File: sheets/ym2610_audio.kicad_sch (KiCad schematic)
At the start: 51 parts, among them J3 SMK S-G8043, U25 NJM2016D, U26 YM3016D, U27 YM2610, U28 RC4558, U29 RC4558, U30 RC4558, U31 RC4558

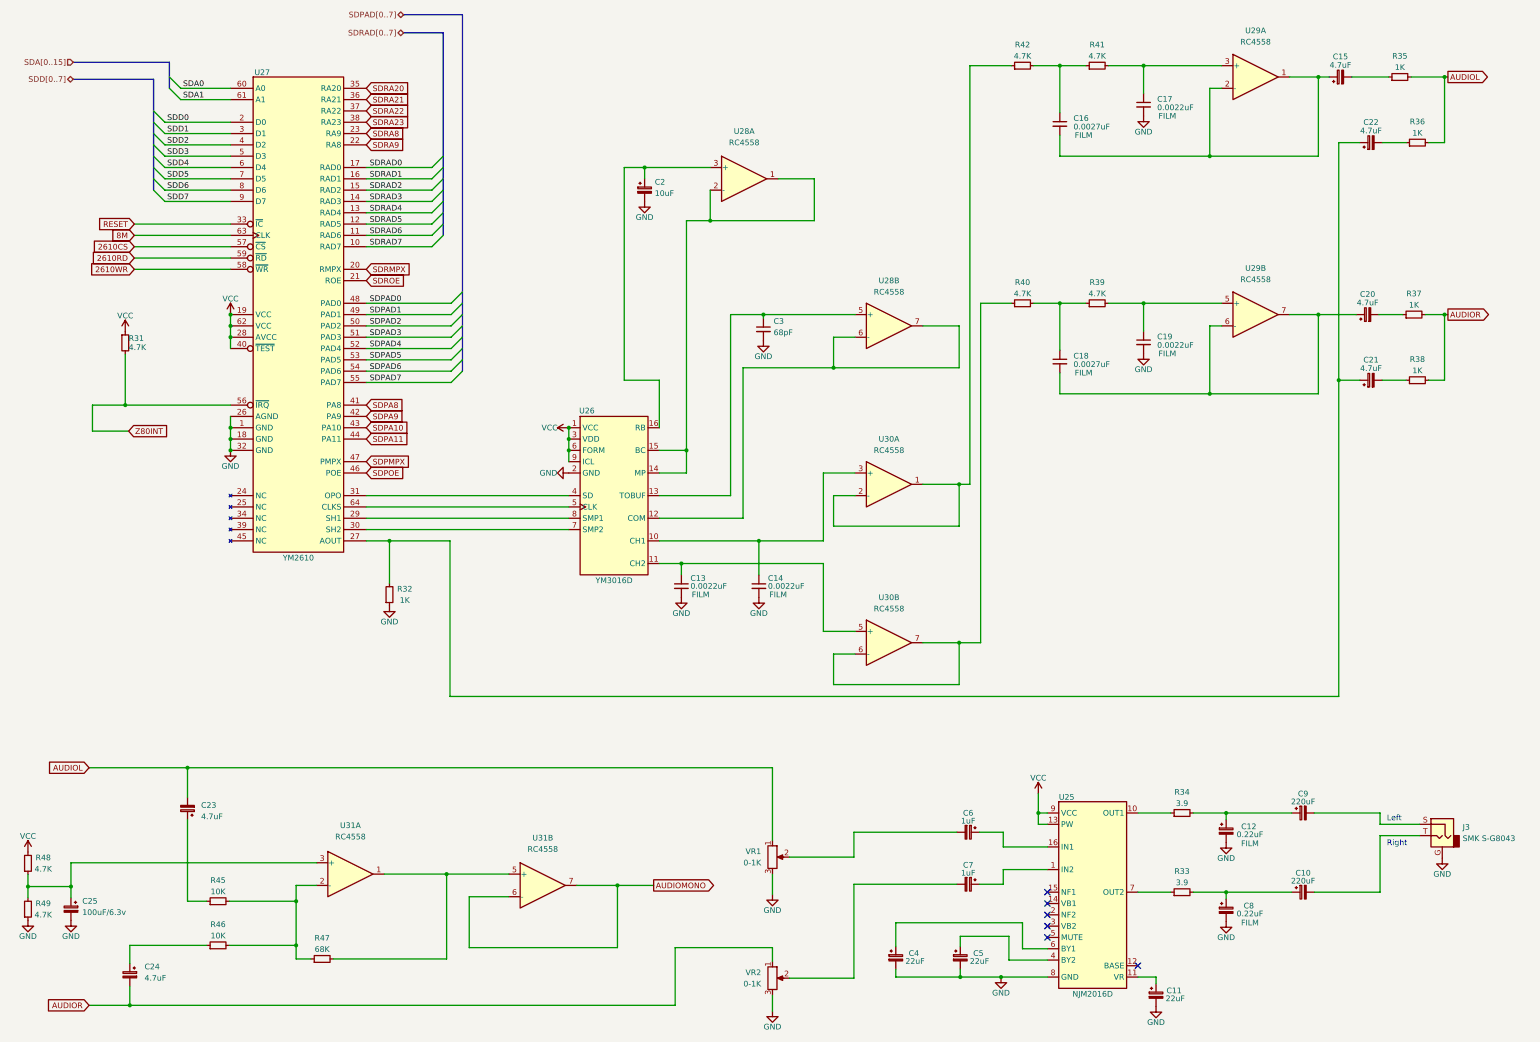
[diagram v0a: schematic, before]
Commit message: Resistor Value Ω added
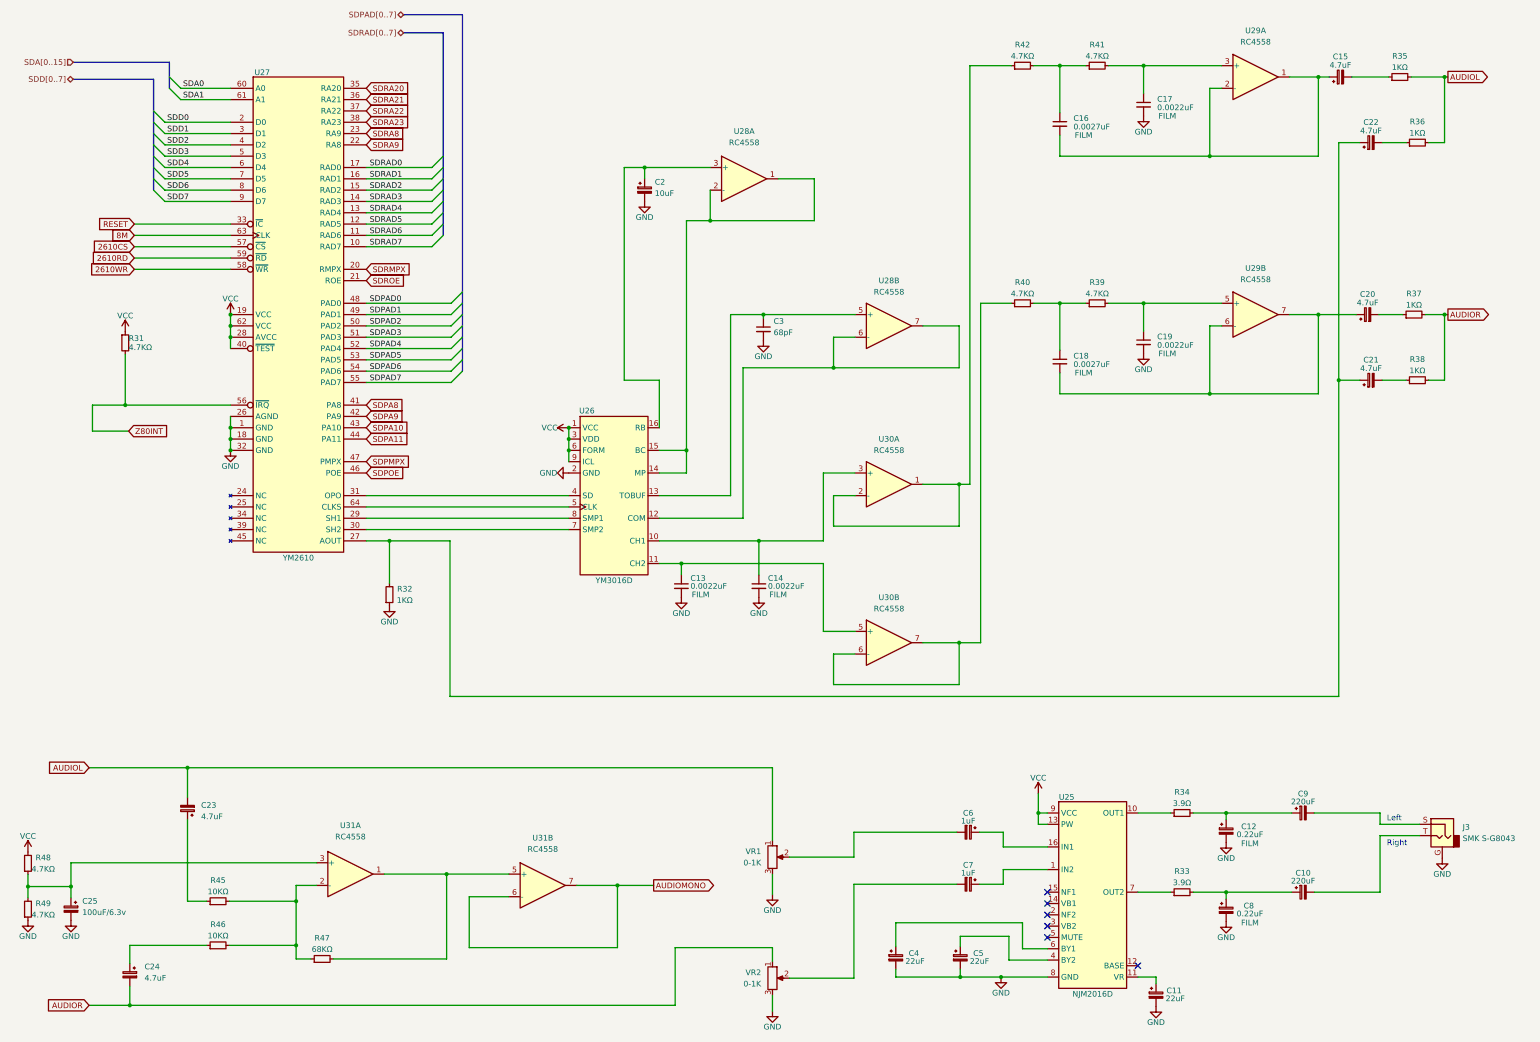
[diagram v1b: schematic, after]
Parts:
- R31, R39, R40, R41, R42, R48, R49: value 4.7K -> 4.7KΩ
- R32, R35, R36, R37, R38: value 1K -> 1KΩ
- R33, R34: value 3.9 -> 3.9Ω
- R45, R46: value 10K -> 10KΩ
- R47: value 68K -> 68KΩ
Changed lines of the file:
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@@
     (in_bom yes) (on_board yes)
     (property "Reference" "R45" (id 0) (at 90.424 211.201 90))
-    (property "Value" "10K" (id 1) (at 90.424 213.741 90))
+    (property "Value" "10KΩ" (id 1) (at 90.424 213.741 90))
     (property "Footprint" "" (id 2) (at 90.424 215.9 0)
       (effects (font (size 1.27 1.27)) hide)
@@
     (in_bom yes) (on_board yes)
     (property "Reference" "R36" (id 0) (at 359.664 40.894 90))
-    (property "Value" "1K" (id 1) (at 359.664 43.434 90))
+    (property "Value" "1KΩ" (id 1) (at 359.664 43.434 90))
     (property "Footprint" "" (id 2) (at 359.664 45.593 0)
       (effects (font (size 1.27 1.27)) hide)
@@
     (in_bom yes) (on_board yes)
     (property "Reference" "R37" (id 0) (at 358.902 79.502 90))
-    (property "Value" "1K" (id 1) (at 358.902 82.042 90))
+    (property "Value" "1KΩ" (id 1) (at 358.902 82.042 90))
     (property "Footprint" "" (id 2) (at 358.902 84.201 0)
       (effects (font (size 1.27 1.27)) hide)
@@
     (in_bom yes) (on_board yes)
     (property "Reference" "R38" (id 0) (at 359.664 94.234 90))
-    (property "Value" "1K" (id 1) (at 359.664 96.774 90))
+    (property "Value" "1KΩ" (id 1) (at 359.664 96.774 90))
     (property "Footprint" "" (id 2) (at 359.664 98.933 0)
       (effects (font (size 1.27 1.27)) hide)
@@
     (in_bom yes) (on_board yes)
     (property "Reference" "R47" (id 0) (at 113.792 224.155 90))
-    (property "Value" "68K" (id 1) (at 113.792 226.695 90))
+    (property "Value" "68KΩ" (id 1) (at 113.792 226.695 90))
     (property "Footprint" "" (id 2) (at 113.792 228.854 0)
       (effects (font (size 1.27 1.27)) hide)
@@
     (in_bom yes) (on_board yes)
     (property "Reference" "R42" (id 0) (at 271.018 23.622 90))
-    (property "Value" "4.7K" (id 1) (at 271.018 26.162 90))
+    (property "Value" "4.7KΩ" (id 1) (at 271.018 26.162 90))
     (property "Footprint" "" (id 2) (at 271.018 28.321 0)
       (effects (font (size 1.27 1.27)) hide)
@@
     (in_bom yes) (on_board yes)
     (property "Reference" "R46" (id 0) (at 90.424 221.107 90))
-    (property "Value" "10K" (id 1) (at 90.424 223.647 90))
+    (property "Value" "10KΩ" (id 1) (at 90.424 223.647 90))
     (property "Footprint" "" (id 2) (at 90.424 225.806 0)
       (effects (font (size 1.27 1.27)) hide)
@@
     (in_bom yes) (on_board yes)
     (property "Reference" "R33" (id 0) (at 306.832 209.169 90))
-    (property "Value" "3.9" (id 1) (at 306.832 211.709 90))
+    (property "Value" "3.9Ω" (id 1) (at 306.832 211.709 90))
     (property "Footprint" "" (id 2) (at 306.832 213.868 0)
       (effects (font (size 1.27 1.27)) hide)
@@
     (in_bom yes) (on_board yes)
     (property "Reference" "R34" (id 0) (at 306.832 191.389 90))
-    (property "Value" "3.9" (id 1) (at 306.832 193.929 90))
+    (property "Value" "3.9Ω" (id 1) (at 306.832 193.929 90))
     (property "Footprint" "" (id 2) (at 306.832 196.088 0)
       (effects (font (size 1.27 1.27)) hide)
@@
     (in_bom yes) (on_board yes)
     (property "Reference" "R40" (id 0) (at 271.018 76.962 90))
-    (property "Value" "4.7K" (id 1) (at 271.018 79.502 90))
+    (property "Value" "4.7KΩ" (id 1) (at 271.018 79.502 90))
     (property "Footprint" "" (id 2) (at 271.018 81.661 0)
       (effects (font (size 1.27 1.27)) hide)
@@
       (effects (font (size 1.27 1.27)) (justify left))
     )
-    (property "Value" "4.7K" (id 1) (at 70.358 91.567 0)
+    (property "Value" "4.7KΩ" (id 1) (at 70.358 91.567 0)
       (effects (font (size 1.27 1.27)) (justify left))
     )
@@
     (in_bom yes) (on_board yes)
     (property "Reference" "R39" (id 0) (at 287.782 76.962 90))
-    (property "Value" "4.7K" (id 1) (at 287.782 79.502 90))
+    (property "Value" "4.7KΩ" (id 1) (at 287.782 79.502 90))
     (property "Footprint" "" (id 2) (at 287.782 81.661 0)
       (effects (font (size 1.27 1.27)) hide)
@@
     (in_bom yes) (on_board yes)
     (property "Reference" "R41" (id 0) (at 287.782 23.622 90))
-    (property "Value" "4.7K" (id 1) (at 287.782 26.162 90))
+    (property "Value" "4.7KΩ" (id 1) (at 287.782 26.162 90))
     (property "Footprint" "" (id 2) (at 287.782 28.321 0)
       (effects (font (size 1.27 1.27)) hide)
@@
     (in_bom yes) (on_board yes)
     (property "Reference" "R48" (id 0) (at 51.181 206.121 0))
-    (property "Value" "4.7K" (id 1) (at 51.181 208.661 0))
+    (property "Value" "4.7KΩ" (id 1) (at 51.181 208.661 0))
     (property "Footprint" "" (id 2) (at 47.752 207.391 0)
       (effects (font (size 1.27 1.27)) hide)
@@
     (in_bom yes) (on_board yes)
     (property "Reference" "R32" (id 0) (at 132.334 145.796 0))
-    (property "Value" "1K" (id 1) (at 132.334 148.336 0))
+    (property "Value" "1KΩ" (id 1) (at 132.334 148.336 0))
     (property "Footprint" "" (id 2) (at 128.905 147.066 0)
       (effects (font (size 1.27 1.27)) hide)
@@
     (in_bom yes) (on_board yes)
     (property "Reference" "R35" (id 0) (at 355.727 26.162 90))
-    (property "Value" "1K" (id 1) (at 355.727 28.702 90))
+    (property "Value" "1KΩ" (id 1) (at 355.727 28.702 90))
     (property "Footprint" "" (id 2) (at 355.727 30.861 0)
       (effects (font (size 1.27 1.27)) hide)
@@
     (in_bom yes) (on_board yes)
     (property "Reference" "R49" (id 0) (at 51.181 216.408 0))
-    (property "Value" "4.7K" (id 1) (at 51.181 218.948 0))
+    (property "Value" "4.7KΩ" (id 1) (at 51.181 218.948 0))
     (property "Footprint" "" (id 2) (at 47.752 217.678 0)
       (effects (font (size 1.27 1.27)) hide)

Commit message: Assigning Footprints
Assigned some footprints to some components. Can still be wrong size on caps
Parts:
- C10, C11, C12, C2, C4, C5, C6, C7, C8, C9: footprint (none) -> 1_NeoGeoLibrary:CAP1-5mm
- C13, C14, C15, C16, C17, C18, C19, C20, C21, C22, C23, C24, C25, C3: footprint (none) -> 1_NeoGeoLibrary:CAP3-5mm
- R31, R32, R33, R34, R35, R36, R37, R38, R39, R40, R41, R42, R45, R46, R47, R48, R49: footprint (none) -> 1_NeoGeoLibrary:Resistor1-5mm

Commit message: Updated Footprints
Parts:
- J3: footprint (none) -> Jumper:SolderJumper-2_P1.3mm_Open_Pad1.0x1.5mm
- U25, U26: footprint (none) -> Package_DIP:DIP-16_W7.62mm
- U27: footprint (none) -> Package_DIP:DIP-64_W25.4mm
- U28, U29, U30, U31: footprint (none) -> Package_DIP:DIP-8_W7.62mm
- VR1, VR2: footprint (none) -> Connector_PinSocket_2.54mm:PinSocket_1x03_P2.54mm_Vertical
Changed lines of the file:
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@@
     (property "Reference" "U25" (id 0) (at 280.924 192.532 0))
     (property "Value" "NJM2016D" (id 1) (at 286.766 236.728 0))
-    (property "Footprint" "" (id 2) (at 286.766 218.948 0)
+    (property "Footprint" "Package_DIP:DIP-16_W7.62mm" (id 2) (at 286.766 218.948 0)
       (effects (font (size 1.27 1.27)) hide)
     )
@@
     (property "Reference" "U28" (id 0) (at 241.046 76.581 0))
     (property "Value" "RC4558" (id 1) (at 241.046 79.121 0))
-    (property "Footprint" "" (id 2) (at 241.046 86.741 0)
+    (property "Footprint" "Package_DIP:DIP-8_W7.62mm" (id 2) (at 241.046 86.741 0)
       (effects (font (size 1.27 1.27)) hide)
     )
@@
     (property "Reference" "U30" (id 0) (at 241.046 112.141 0))
     (property "Value" "RC4558" (id 1) (at 241.046 114.681 0))
-    (property "Footprint" "" (id 2) (at 241.046 122.301 0)
+    (property "Footprint" "Package_DIP:DIP-8_W7.62mm" (id 2) (at 241.046 122.301 0)
       (effects (font (size 1.27 1.27)) hide)
     )
@@
     (property "Reference" "U29" (id 0) (at 323.342 20.447 0))
     (property "Value" "RC4558" (id 1) (at 323.342 22.987 0))
-    (property "Footprint" "" (id 2) (at 323.342 30.861 0)
+    (property "Footprint" "Package_DIP:DIP-8_W7.62mm" (id 2) (at 323.342 30.861 0)
       (effects (font (size 1.27 1.27)) hide)
     )
@@
     (property "Reference" "U30" (id 0) (at 241.046 147.701 0))
     (property "Value" "RC4558" (id 1) (at 241.046 150.241 0))
-    (property "Footprint" "" (id 2) (at 241.046 157.861 0)
+    (property "Footprint" "Package_DIP:DIP-8_W7.62mm" (id 2) (at 241.046 157.861 0)
       (effects (font (size 1.27 1.27)) hide)
     )
@@
       (effects (font (size 1.27 1.27)) (justify right))
     )
-    (property "Footprint" "" (id 2) (at 214.884 205.994 0)
+    (property "Footprint" "Connector_PinSocket_2.54mm:PinSocket_1x03_P2.54mm_Vertical" (id 2) (at 214.884 205.994 0)
       (effects (font (size 1.27 1.27)) hide)
     )
@@
     (property "Reference" "U26" (id 0) (at 173.228 105.791 0))
     (property "Value" "YM3016D" (id 1) (at 179.324 143.891 0))
-    (property "Footprint" "" (id 2) (at 179.324 132.461 0)
+    (property "Footprint" "Package_DIP:DIP-16_W7.62mm" (id 2) (at 179.324 132.461 0)
       (effects (font (size 1.27 1.27)) hide)
     )
@@
     (property "Reference" "U29" (id 0) (at 323.342 73.787 0))
     (property "Value" "RC4558" (id 1) (at 323.342 76.327 0))
-    (property "Footprint" "" (id 2) (at 323.342 84.201 0)
+    (property "Footprint" "Package_DIP:DIP-8_W7.62mm" (id 2) (at 323.342 84.201 0)
       (effects (font (size 1.27 1.27)) hide)
     )
@@
     (property "Reference" "U31" (id 0) (at 120.142 198.882 0))
     (property "Value" "RC4558" (id 1) (at 120.142 201.422 0))
-    (property "Footprint" "" (id 2) (at 120.142 209.804 0)
+    (property "Footprint" "Package_DIP:DIP-8_W7.62mm" (id 2) (at 120.142 209.804 0)
       (effects (font (size 1.27 1.27)) hide)
     )
@@
     (property "Reference" "U31" (id 0) (at 163.322 201.676 0))
     (property "Value" "RC4558" (id 1) (at 163.322 204.216 0))
-    (property "Footprint" "" (id 2) (at 163.322 212.344 0)
+    (property "Footprint" "Package_DIP:DIP-8_W7.62mm" (id 2) (at 163.322 212.344 0)
       (effects (font (size 1.27 1.27)) hide)
     )
@@
       (effects (font (size 1.27 1.27)) (justify right))
     )
-    (property "Footprint" "" (id 2) (at 365.252 201.168 0)
+    (property "Footprint" "Jumper:SolderJumper-2_P1.3mm_Open_Pad1.0x1.5mm" (id 2) (at 365.252 201.168 0)
       (effects (font (size 1.27 1.27)) hide)
     )
@@
     (property "Reference" "U28" (id 0) (at 208.534 43.053 0))
     (property "Value" "RC4558" (id 1) (at 208.534 45.593 0))
-    (property "Footprint" "" (id 2) (at 208.534 53.721 0)
+    (property "Footprint" "Package_DIP:DIP-8_W7.62mm" (id 2) (at 208.534 53.721 0)
       (effects (font (size 1.27 1.27)) hide)
     )
@@
       (effects (font (size 1.27 1.27)) (justify right))
     )
-    (property "Footprint" "" (id 2) (at 214.884 233.172 0)
+    (property "Footprint" "Connector_PinSocket_2.54mm:PinSocket_1x03_P2.54mm_Vertical" (id 2) (at 214.884 233.172 0)
       (effects (font (size 1.27 1.27)) hide)
     )
@@
     (property "Reference" "U27" (id 0) (at 100.33 29.845 0))
     (property "Value" "YM2610" (id 1) (at 108.458 138.811 0))
-    (property "Footprint" "" (id 2) (at 108.458 89.281 0)
-      (effects (font (size 1.27 1.27)) hide)
-    )
+    (property "Footprint" "Package_DIP:DIP-64_W25.4mm" (id 2) (at 108.458 89.281 0)
+      (effects (font (size 1.27 1.27)) hide)
+    )
